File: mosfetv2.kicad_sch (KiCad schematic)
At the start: 25 parts, among them Q10 STL90N6F7, Q11 STL90N6F7, Q12 STL90N6F7, Q7 STL90N6F7, Q8 STL90N6F7, Q9 STL90N6F7

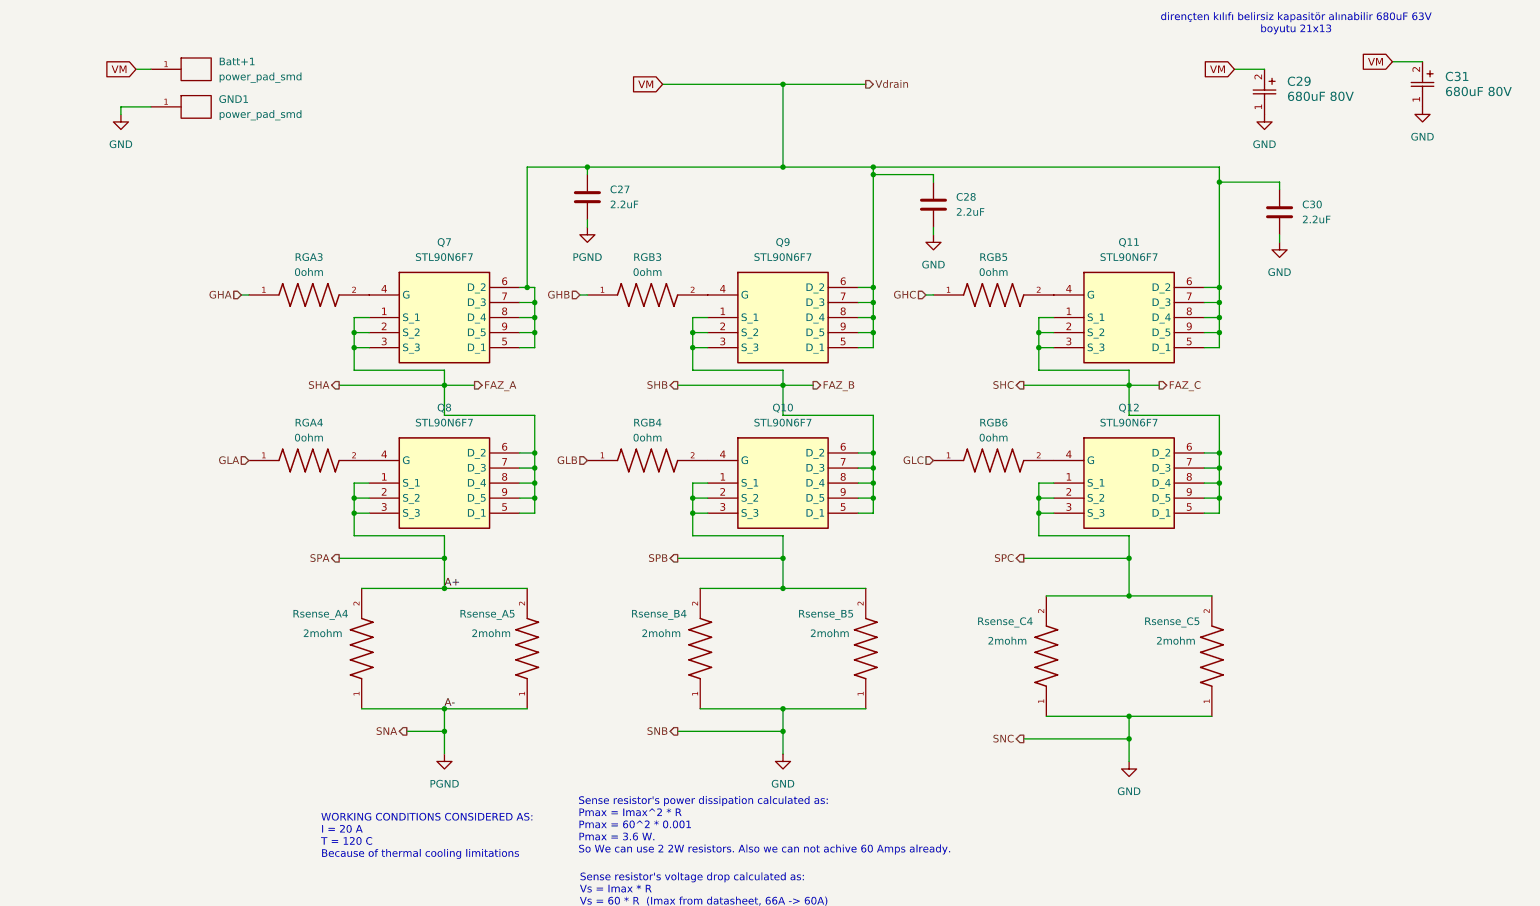
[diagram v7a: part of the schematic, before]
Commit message: Some pcb design and schematics editings about PGND_DRV
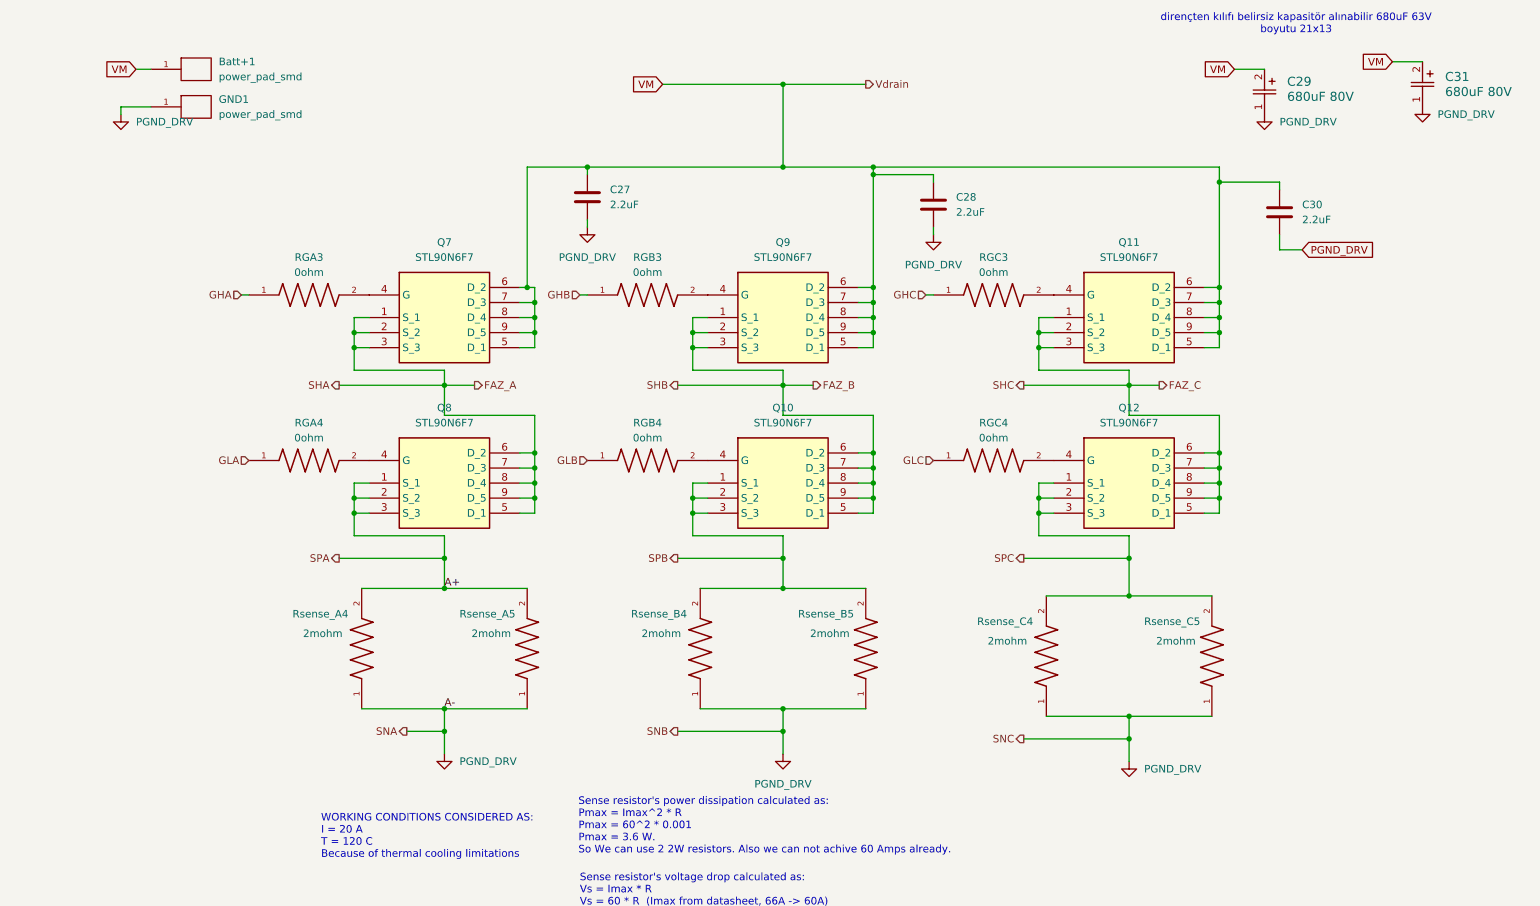
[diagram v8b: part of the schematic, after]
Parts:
- renumbered RGB5 to RGC3, RGB6 to RGC4
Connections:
- net PGND is gone; now on net PGND_DRV: C27.2, Rsense_A4.1, Rsense_A5.1
- net GND renamed PGND_DRV
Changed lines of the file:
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@@
 	(wire
 		(pts
+			(xy 241.3 57.15) (xy 245.11 57.15)
+		)
+		(stroke
+			(width 0)
+			(type default)
+		)
+	)
+	(wire
+		(pts
 			(xy 85.09 71.12) (xy 85.09 73.66)
 		)
@@
 	(wire
 		(pts
-			(xy 241.3 54.61) (xy 241.3 55.88)
+			(xy 241.3 54.61) (xy 241.3 57.15)
 		)
 		(stroke
@@
 		)
 	)
+	(global_label "PGND_DRV"
+		(shape input)
+		(at 245.11 57.15 0)
+		(fields_autoplaced yes)
+		(effects
+			(font
+				(size 1.27 1.27)
+			)
+			(justify left)
+		)
+		(property "Intersheetrefs" "${INTERSHEET_REFS}"
+			(at 257.8319 57.15 0)
+			(effects
+				(font
+					(size 1.27 1.27)
+				)
+				(justify left)
+				(hide yes)
+			)
+		)
+	)
 	(global_label "VM"
 		(shape input)
@@
 			)
 		)
-		(property "Value" "GND"
+		(property "Value" "PGND_DRV"
 			(at 182.88 59.69 0)
 			(effects
@@
 			)
 		)
-		(property "Value" "GND"
-			(at 238.76 39.37 0)
+		(property "Value" "PGND_DRV"
+			(at 241.3 35.5599 0)
 			(effects
 				(font
 					(size 1.27 1.27)
 				)
+				(justify left)
 			)
 		)
@@
 			)
 		)
-		(property "Value" "GND"
-			(at 265.43 38.1 0)
+		(property "Value" "PGND_DRV"
+			(at 267.97 34.2899 0)
 			(effects
 				(font
 					(size 1.27 1.27)
 				)
+				(justify left)
 			)
 		)
@@
 		(dnp no)
 		(fields_autoplaced yes)
-		(property "Reference" "RGB6"
+		(property "Reference" "RGC4"
 			(at 193.04 86.36 0)
 			(effects
@@
 			(project "Ana_ESC"
 				(path "/57129761-6d47-486c-bd7a-90dbb6f75754/a2e9c01f-dc3c-42e3-9ad2-b4c7bc962bba"
-					(reference "RGB6")
+					(reference "RGC4")
 					(unit 1)
 				)
@@
 			)
 		)
-		(property "Value" "GND"
+		(property "Value" "PGND_DRV"
 			(at 157.48 147.32 0)
 			(effects
@@
 		(dnp no)
 		(fields_autoplaced yes)
-		(property "Reference" "RGB5"
+		(property "Reference" "RGC3"
 			(at 193.04 58.42 0)
 			(effects
@@
 			(project "Ana_ESC"
 				(path "/57129761-6d47-486c-bd7a-90dbb6f75754/a2e9c01f-dc3c-42e3-9ad2-b4c7bc962bba"
-					(reference "RGB5")
+					(reference "RGC3")
 					(unit 1)
 				)
@@
 	)
 	(symbol
-		(lib_id "power:GND")
-		(at 241.3 55.88 0)
-		(unit 1)
-		(exclude_from_sim no)
-		(in_bom yes)
-		(on_board yes)
-		(dnp no)
-		(fields_autoplaced yes)
-		(property "Reference" "#PWR0102"
-			(at 241.3 62.23 0)
-			(effects
-				(font
-					(size 1.27 1.27)
-				)
-				(hide yes)
-			)
-		)
-		(property "Value" "GND"
-			(at 241.3 60.96 0)
-			(effects
-				(font
-					(size 1.27 1.27)
-				)
-			)
-		)
-		(property "Footprint" ""
-			(at 241.3 55.88 0)
-			(effects
-				(font
-					(size 1.27 1.27)
-				)
-				(hide yes)
-			)
-		)
-		(property "Datasheet" ""
-			(at 241.3 55.88 0)
-			(effects
-				(font
-					(size 1.27 1.27)
-				)
-				(hide yes)
-			)
-		)
-		(property "Description" "Power symbol creates a global label with name \"GND\" , ground"
-			(at 241.3 55.88 0)
-			(effects
-				(font
-					(size 1.27 1.27)
-				)
-				(hide yes)
-			)
-		)
-		(pin "1"
-		)
-		(instances
-			(project "Ana_ESC"
-				(path "/57129761-6d47-486c-bd7a-90dbb6f75754/a2e9c01f-dc3c-42e3-9ad2-b4c7bc962bba"
-					(reference "#PWR0102")
-					(unit 1)
-				)
-			)
-		)
-	)
-	(symbol
 		(lib_name "STL90N6F7_1")
 		(lib_id "STL90N6F7:STL90N6F7")
@@
 			)
 		)
-		(property "Value" "GND"
-			(at 45.72 39.37 0)
+		(property "Value" "PGND_DRV"
+			(at 48.26 35.5599 0)
 			(effects
 				(font
 					(size 1.27 1.27)
 				)
+				(justify left)
 			)
 		)
@@
 			)
 		)
-		(property "Value" "GND"
-			(at 215.9 148.59 0)
+		(property "Value" "PGND_DRV"
+			(at 218.44 144.7799 0)
 			(effects
 				(font
 					(size 1.27 1.27)
 				)
+				(justify left)
 			)
 		)
@@
 			)
 		)
-		(property "Value" "PGND"
-			(at 100.33 147.32 0)
+		(property "Value" "PGND_DRV"
+			(at 102.87 143.5099 0)
 			(effects
 				(font
 					(size 1.27 1.27)
 				)
+				(justify left)
 			)
 		)
@@
 			)
 		)
-		(property "Value" "PGND"
+		(property "Value" "PGND_DRV"
 			(at 124.46 58.42 0)
 			(effects
